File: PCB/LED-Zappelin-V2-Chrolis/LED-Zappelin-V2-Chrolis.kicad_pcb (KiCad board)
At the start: 2 copper layers, 120 x 100 mm, 30 parts, among them J1 Blanking Signal, J2 Trigger, J3 Chrolis 1, J4 Chrolis 2, J5 NeoPixel Strip, Q1 2N5089, Q2 2N5089, SW1 Blanking Switch, SW2 Blanking Inverter Switch, U1 ESP32-DEVKITC-32D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

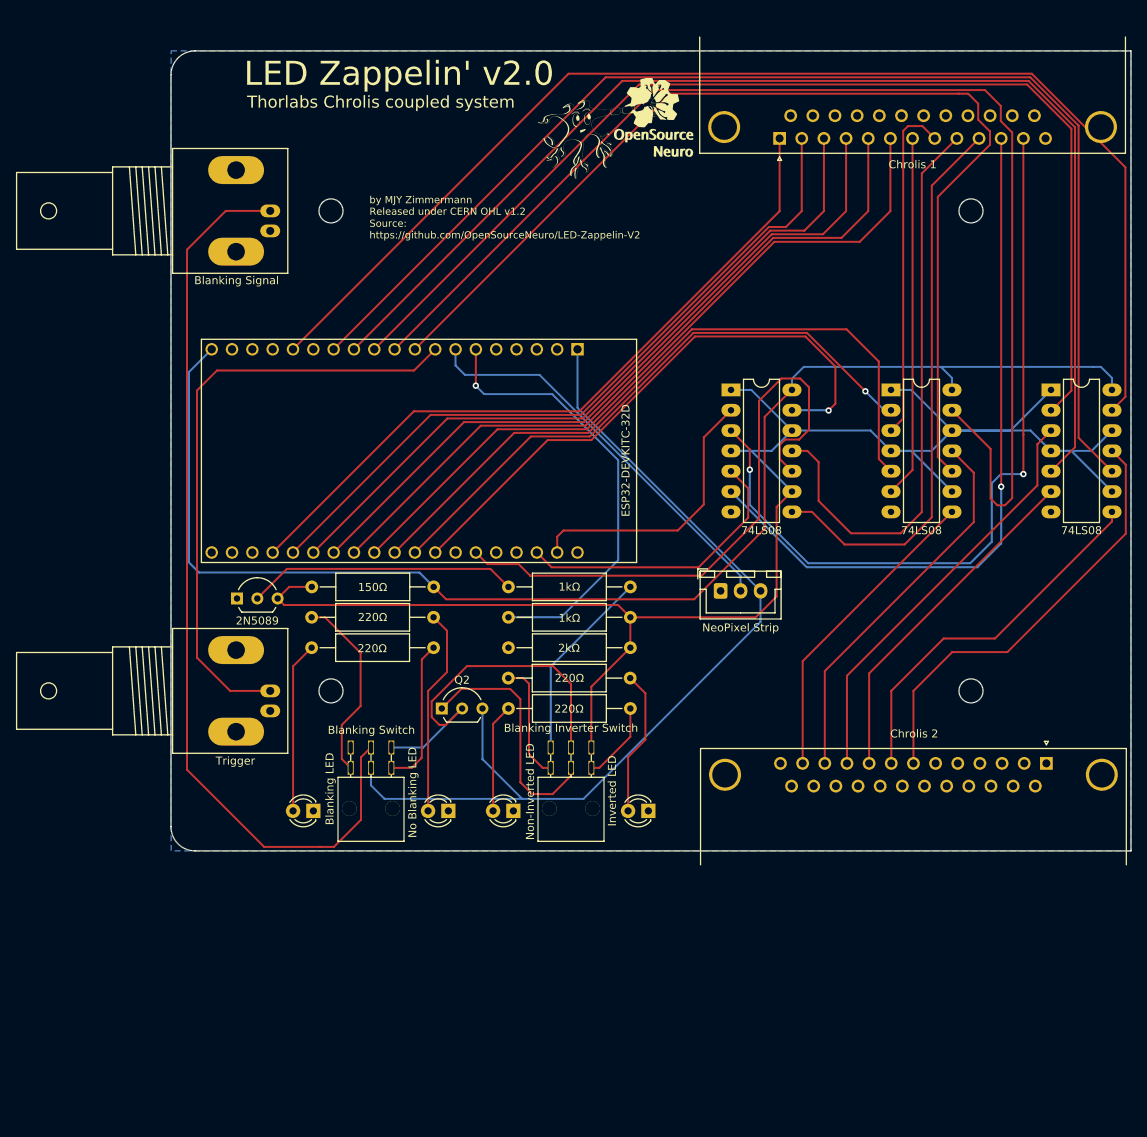
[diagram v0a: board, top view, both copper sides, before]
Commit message: update board for chrolis
This update adds a voltage regulator to the board, as well as a connection to an external power supply. Footprints have been moved around so that only two sides of the board have connectors.
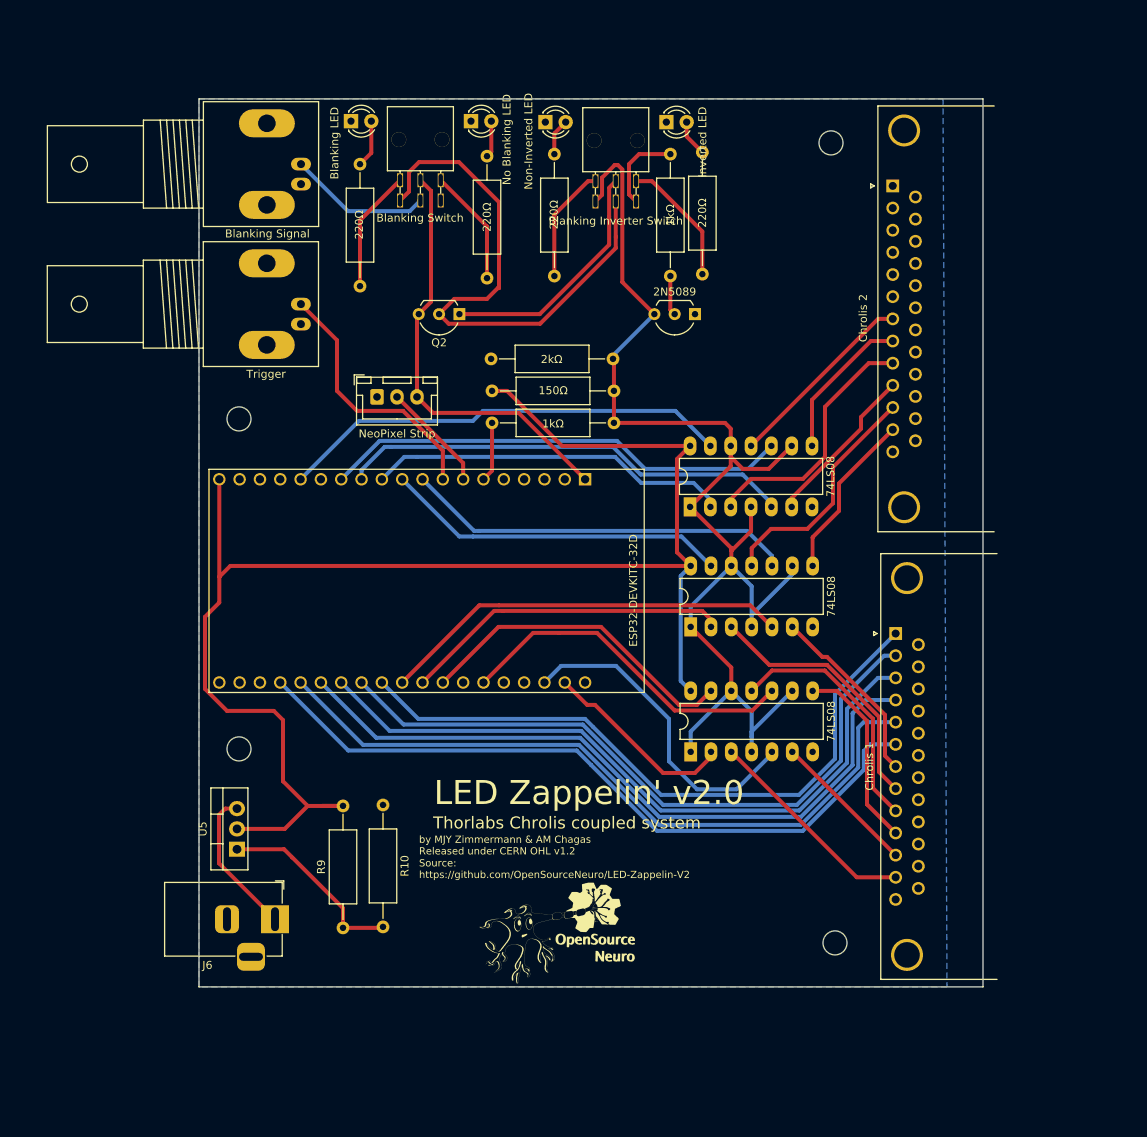
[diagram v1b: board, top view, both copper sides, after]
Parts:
- added J6: Barrel_Jack, Connector_BarrelJack:BarrelJack_Horizontal, F.Cu at (63.0, 143.4)
- added R10: 330, Resistor_THT:R_Axial_DIN0309_L9.0mm_D3.2mm_P15.24mm_Horizontal, F.Cu at (76.5, 129.1)
- added R9: 1k, Resistor_THT:R_Axial_DIN0309_L9.0mm_D3.2mm_P15.24mm_Horizontal, F.Cu at (71.5, 144.5)
- added U5: LM317_TO-220, Package_TO_SOT_THT:TO-220-3_Vertical, F.Cu at (58.2, 134.6)
- moved ? 100.9 mm to (98.0, 145.1)
- moved SW1 92.0 mm to (81.1, 41.8), turned to 180 degrees
- moved SW2 91.9 mm to (105.5, 42.0), turned to 180 degrees
- moved D1 86.3 mm to (72.5, 43.6), turned to 0 degrees
- moved D2 86.3 mm to (87.5, 43.6), turned to 0 degrees
- moved D4 86.2 mm to (96.7, 43.8), turned to 0 degrees
- moved D3 86.1 mm to (111.9, 43.8), turned to 0 degrees
- moved J4 74.7 mm to (140.2, 51.7), turned to 90 degrees
- moved R8 69.5 mm to (97.9, 47.8), turned to -90 degrees
- moved Q1 67.4 mm to (115.5, 67.8), turned to 180 degrees
- moved R7 66.4 mm to (116.4, 47.5), turned to -90 degrees
- moved J3 63.6 mm to (140.5, 107.7), turned to 90 degrees
- moved R3 60.7 mm to (73.6, 49.0), turned to -90 degrees
- moved R4 58.0 mm to (89.5, 48.0), turned to -90 degrees
- moved Q2 49.3 mm to (86.0, 67.8), turned to 180 degrees
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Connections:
- J3 pad 1: GPIO15 -> GPIO17
- J3 pad 2: GPIO02 -> GPIO16
- J3 pad 3: GPIO00 -> GPIO04
- J3 pad 4: GPIO04 -> GPIO00
- J3 pad 5: GPIO16 -> GPIO02
- J3 pad 6: GPIO17 -> GPIO15
- U4 pad 3: GPIO Input 9 -> GPIO Input 10
- U4 pad 6: GPIO Input 10 -> GPIO Input 9
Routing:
- net GPIO26: track 156.1 -> 43.1 mm
- net GPIO13: track 154.2 -> 56.6 mm
- net Net-(J1-In): track 114.4 -> 18.0 mm
- net GPIO12: track 154.6 -> 58.4 mm
- net GPIO27: track 139.5 -> 44.4 mm
- net GPIO28: track 150.7 -> 56.5 mm
- net GPIO25: track 134.2 -> 48.9 mm
- net GPIO Input 1: track 98.5 -> 27.0 mm, vias 2 -> 0
- net GPIO Input 2: track 89.6 -> 18.3 mm, vias 1 -> 0
- net 3.3V: track 117.7 -> 53.6 mm
- net Blanking: track 217.5 -> 158.7 mm
- net Net-(U1-IO35): track 55.4 -> 7.49 mm, vias 1 -> 0
- net GPIO Input 3: track 70.4 -> 23.8 mm
- net Trigger: track 76.2 -> 32.6 mm
- net GPIO Input 4: track 73.0 -> 31.4 mm
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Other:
- board size 120 x 100 mm -> 98 x 111 mm
- board text added: "by MJY Zimmermann & AM Chagas Released under CERN OHL v1.2"
- board text removed: "by MJY Zimmermann Released under CERN OHL v1.2"

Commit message: update PCB
Previous modifications were kept, transistor Q2 was rerouted to sw1 pin6, all power line are now linked to external 5v power supply.
PCB was rearranged to accommodate box equipment. The neopixel strip for example requires 110mm +some tolerance on one side
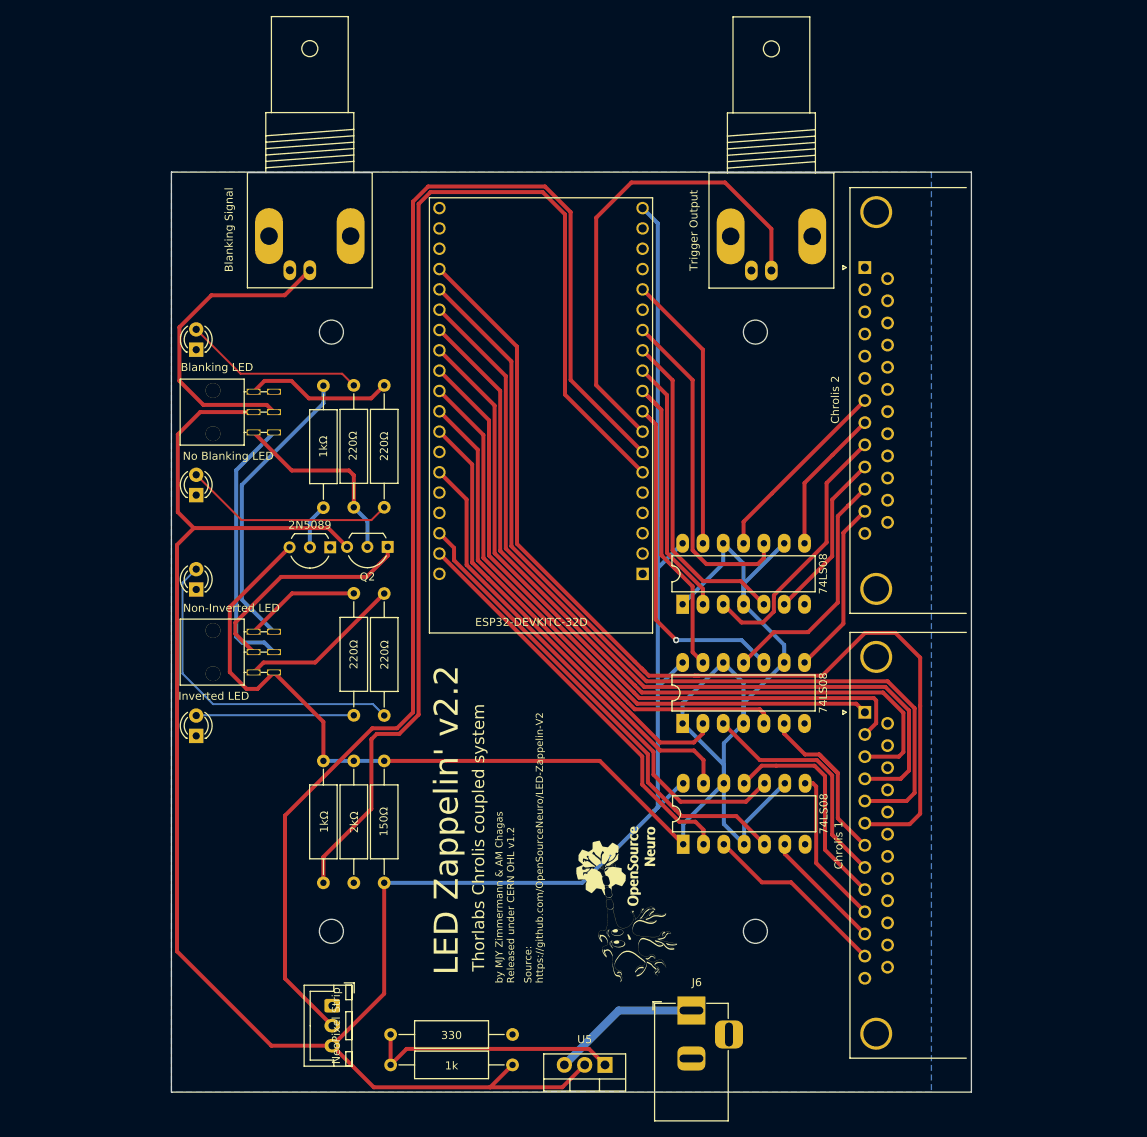
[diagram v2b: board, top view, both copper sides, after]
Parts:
- J2: value Trigger -> Trigger Output
- moved D3 96.6 mm to (53.1, 120.5), turned to 90 degrees
- moved SW2 87.1 mm to (51.1, 110.0), turned to -90 degrees
- moved R7 82.8 mm to (72.8, 117.9), turned to 90 degrees
- moved J5 76.3 mm to (70.1, 154.2), turned to -90 degrees
- moved R8 73.3 mm to (76.6, 117.9), turned to 90 degrees
- moved D4 72.9 mm to (53.1, 102.2), turned to 90 degrees
- moved R2 67.7 mm to (72.8, 138.8), turned to 90 degrees
- moved J2 64.5 mm to (125.0, 57.3), turned to 0 degrees
- moved R1 61.2 mm to (69.0, 138.8), turned to 90 degrees
- moved D2 58.0 mm to (53.1, 90.4), turned to 90 degrees
- moved R5 54.4 mm to (76.6, 123.6), turned to -90 degrees
- moved Q1 54.1 mm to (69.8, 96.9)
- moved U5 53.3 mm to (104.2, 161.6), turned to 180 degrees
- moved J6 53.3 mm to (115.0, 154.8), turned to 90 degrees
- moved R6 52.1 mm to (69.0, 91.9)
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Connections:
- J5 pad 3: 3.3V -> 5V
- Q2 pad 3: 3.3V -> 5V
- R3 pad 2: Net-(R3-Pad2) -> Net-(Q2-B)
- SW1 pad 3: Net-(Q2-B) -> Net-(SW1-C-Pad3)
- SW1 pad 5: 3.3V -> 5V
- SW1 pad 6: Net-(R3-Pad2) -> Net-(Q2-B)
- SW2 pad 2: Net-(Q2-B) -> Net-(SW1-C-Pad3)
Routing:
- net NeoPixel: track 13.7 -> 169.4 mm
- net Net-(U1-IO35): track 7.49 -> 147.7 mm
- net 5V: track 187.5 -> 313.3 mm
- net 3.3V: track 53.6 -> 0.00 mm
- net Net-(Q2-B): track 69.8 -> 24.4 mm
- net Blanking: track 158.7 -> 200.7 mm
- net GPIO15: track 90.5 -> 127.3 mm
- net Net-(D4-A): track 4.59 -> 41.1 mm
- net Net-(SW1-C-Pad3): track 0.00 -> 33.0 mm
- net Trigger: track 32.6 -> 60.5 mm
- net GPIO23: track 23.8 -> 51.5 mm
- net Net-(R6-Pad2): track 10.7 -> 36.7 mm
- net Net-(D2-A): track 4.60 -> 26.5 mm
- net GPIO02: track 90.0 -> 111.8 mm
- net GPIO13: track 56.6 -> 34.9 mm
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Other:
- board size 98 x 111 mm -> 100 x 115 mm
- board text added: "LED Zappelin' v2.2"
- board text removed: "LED Zappelin' v2.0"

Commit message: update PCB
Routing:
- net 5V: track 313.3 -> 367.8 mm
- net GPIO25: track 44.3 -> 46.6 mm, vias 1 -> 0
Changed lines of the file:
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@@
   (segment (start 53.6 80) (end 60.28 80) (width 0.5) (layer "F.Cu") (net 39))
   (segment (start 50.7 132.5) (end 50.7 147.4) (width 0.5) (layer "F.Cu") (net 39))
-  (segment (start 110.8 114.9) (end 110.8 114.4) (width 0.5) (layer "B.Cu") (net 39))
-  (segment (start 110.8 100.4) (end 110.8 114.9) (width 0.5) (layer "B.Cu") (net 39))
-  (segment (start 110.8 100.4) (end 110.8 99.1) (width 0.5) (layer "B.Cu") (net 39))
-  (segment (start 110.8 56.4) (end 108.9 54.5) (width 0.5) (layer "B.Cu") (net 39))
-  (segment (start 110.8 99.5) (end 113.9 96.4) (width 0.5) (layer "B.Cu") (net 39))
-  (segment (start 110.8 114.9) (end 110.8 129.4) (width 0.5) (layer "B.Cu") (net 39))
-  (segment (start 110.8 100.4) (end 110.8 99.5) (width 0.5) (layer "B.Cu") (net 39))
-  (segment (start 110.35 129.85) (end 101.36 138.84) (width 0.5) (layer "B.Cu") (net 39))
+  (segment (start 105.1 104.08995) (end 105.1 101.2) (width 0.5) (layer "B.Cu") (net 39))
+  (segment (start 105.1 58.3) (end 105.1 101.2) (width 0.5) (layer "B.Cu") (net 39))
+  (segment (start 113.975 126.4) (end 105.275 135.1) (width 0.5) (layer "B.Cu") (net 39))
+  (segment (start 108.9 54.5) (end 113.9 59.5) (width 0.5) (layer "B.Cu") (net 39))
+  (segment (start 113.9 59.5) (end 113.9 96.4) (width 0.5) (layer "B.Cu") (net 39))
+  (segment (start 104.65 135.55) (end 101.36 138.84) (width 0.5) (layer "B.Cu") (net 39))
   (segment (start 101.36 138.84) (end 76.6 138.84) (width 0.5) (layer "B.Cu") (net 39))
-  (segment (start 110.8 99.1) (end 110.8 56.4) (width 0.5) (layer "B.Cu") (net 39))
-  (segment (start 110.8 114.4) (end 113.9 111.3) (width 0.5) (layer "B.Cu") (net 39))
+  (segment (start 112.31005 111.3) (end 105.1 104.08995) (width 0.5) (layer "B.Cu") (net 39))
+  (segment (start 105.275 135.1) (end 105.1 135.1) (width 0.5) (layer "B.Cu") (net 39))
+  (segment (start 105.1 101.2) (end 105.1 135.1) (width 0.5) (layer "B.Cu") (net 39))
+  (segment (start 105.1 135.1) (end 104.65 135.55) (width 0.5) (layer "B.Cu") (net 39))
+  (segment (start 113.9 111.3) (end 112.31005 111.3) (width 0.5) (layer "B.Cu") (net 39))
   (segment (start 113.8 126.4) (end 113.975 126.4) (width 0.5) (layer "B.Cu") (net 39))
-  (segment (start 110.35 129.85) (end 113.8 126.4) (width 0.5) (layer "B.Cu") (net 39))
-  (segment (start 110.8 129.4) (end 110.35 129.85) (width 0.5) (layer "B.Cu") (net 39))
+  (segment (start 108.9 54.5) (end 105.1 58.3) (width 0.5) (layer "B.Cu") (net 39))
   (segment (start 69 78.9) (end 69 76.7) (width 0.5) (layer "B.Cu") (net 40))
   (segment (start 58.8 89.1) (end 69 78.9) (width 0.5) (layer "B.Cu") (net 40))
@@
   (segment (start 102.2 159.6) (end 104.2 161.6) (width 0.5) (layer "F.Cu") (net 46))
   (segment (start 77.4 161.6) (end 79.4 159.6) (width 0.5) (layer "F.Cu") (net 46))
-  (segment (start 108.9 79.9) (end 110.55 81.55) (width 0.5) (layer "F.Cu") (net 49))
-  (segment (start 108.9 79.9) (end 110.2 81.2) (width 0.5) (layer "F.Cu") (net 49))
-  (segment (start 110.55 81.55) (end 110.55 105.95) (width 0.5) (layer "F.Cu") (net 49))
-  (segment (start 110.55 105.95) (end 113.1 108.5) (width 0.5) (layer "F.Cu") (net 49))
-  (via (at 113.1 108.5) (size 0.8) (drill 0.4) (layers "F.Cu" "B.Cu") (net 49))
-  (segment (start 121.26 108.5) (end 113.1 108.5) (width 0.5) (layer "B.Cu") (net 49))
   (segment (start 124.06 111.3) (end 121.26 108.5) (width 0.5) (layer "B.Cu") (net 49))
+  (segment (start 105.8 83) (end 108.9 79.9) (width 0.5) (layer "B.Cu") (net 49))
+  (segment (start 121.26 108.5) (end 110.5 108.5) (width 0.5) (layer "B.Cu") (net 49))
+  (segment (start 110.5 108.5) (end 105.8 103.8) (width 0.5) (layer "B.Cu") (net 49))
+  (segment (start 105.8 103.8) (end 105.8 83) (width 0.5) (layer "B.Cu") (net 49))
   (segment (start 108.9 77.36) (end 110.6 79.06) (width 0.5) (layer "F.Cu") (net 50))
   (segment (start 108.9 77.36) (end 110.85 79.31) (width 0.5) (layer "F.Cu") (net 50))
